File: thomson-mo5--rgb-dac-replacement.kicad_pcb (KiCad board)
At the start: 2 copper layers, 0 parts

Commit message: Done PCB
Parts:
- added J1: Input, Connector_PinHeader_2.54mm:PinHeader_1x09_P2.54mm_Vertical, F.Cu at (158.8, 76.2)
- added J2: Output, Connector_PinHeader_2.54mm:PinHeader_1x03_P2.54mm_Vertical, F.Cu at (74.9, 78.7)
- added Q1: 2N3904, Package_TO_SOT_THT:TO-92_Inline_Wide, F.Cu at (125.7, 99.1)
- added Q2: 2N3904, Package_TO_SOT_THT:TO-92_Inline_Wide, F.Cu at (110.5, 99.1)
- added Q3: 2N3904, Package_TO_SOT_THT:TO-92_Inline_Wide, F.Cu at (95.2, 99.1)
- added R1: 1K5, commons-passives_THT:Passive_THT_resistor_W2.54mm_L12.70mm, F.Cu at (130.8, 85.1)
- added R10: 3K, commons-passives_THT:Passive_THT_resistor_W2.54mm_L12.70mm, F.Cu at (102.9, 85.1)
- added R11: 6K2, commons-passives_THT:Passive_THT_resistor_W2.54mm_L12.70mm, F.Cu at (100.3, 85.1)
- added R12: 12K, commons-passives_THT:Passive_THT_resistor_W2.54mm_L12.70mm, F.Cu at (97.8, 85.1)
- added R13: 1K, commons-passives_THT:Passive_THT_resistor_W2.54mm_L12.70mm, F.Cu at (132.1, 103.5)
- added R14: 1K, commons-passives_THT:Passive_THT_resistor_W2.54mm_L12.70mm, F.Cu at (116.8, 103.5)
- added R15: 1K, commons-passives_THT:Passive_THT_resistor_W2.54mm_L12.70mm, F.Cu at (101.6, 103.5)
- added R16: 2K, commons-passives_THT:Passive_THT_resistor_W2.54mm_L12.70mm, F.Cu at (132.1, 106.0)
- added R17: 2K, commons-passives_THT:Passive_THT_resistor_W2.54mm_L12.70mm, F.Cu at (116.8, 106.0)
- added R18: 2K, commons-passives_THT:Passive_THT_resistor_W2.54mm_L12.70mm, F.Cu at (101.6, 106.0)
- added R19: 150, commons-passives_THT:Passive_THT_resistor_W2.54mm_L12.70mm, F.Cu at (132.1, 108.6)
- added R2: 3K, commons-passives_THT:Passive_THT_resistor_W2.54mm_L12.70mm, F.Cu at (128.3, 85.1)
- added R20: 150, commons-passives_THT:Passive_THT_resistor_W2.54mm_L12.70mm, F.Cu at (116.8, 108.6)
- added R21: 150, commons-passives_THT:Passive_THT_resistor_W2.54mm_L12.70mm, F.Cu at (101.6, 108.6)
- added R22: 75, commons-passives_THT:Passive_THT_resistor_W2.54mm_L12.70mm, F.Cu at (92.7, 85.1)
- added R23: 75, commons-passives_THT:Passive_THT_resistor_W2.54mm_L12.70mm, F.Cu at (90.2, 85.1)
- added R24: 75, commons-passives_THT:Passive_THT_resistor_W2.54mm_L12.70mm, F.Cu at (87.6, 85.1)
- added R3: 6K2, commons-passives_THT:Passive_THT_resistor_W2.54mm_L12.70mm, F.Cu at (125.7, 85.1)
- added R4: 12K, commons-passives_THT:Passive_THT_resistor_W2.54mm_L12.70mm, F.Cu at (123.2, 85.1)
- added R5: 1K5, commons-passives_THT:Passive_THT_resistor_W2.54mm_L12.70mm, F.Cu at (118.1, 85.1)
- added R6: 3K, commons-passives_THT:Passive_THT_resistor_W2.54mm_L12.70mm, F.Cu at (115.6, 85.1)
- added R7: 6K2, commons-passives_THT:Passive_THT_resistor_W2.54mm_L12.70mm, F.Cu at (113.0, 85.1)
- added R8: 12K, commons-passives_THT:Passive_THT_resistor_W2.54mm_L12.70mm, F.Cu at (110.5, 85.1)
- added R9: 1K5, commons-passives_THT:Passive_THT_resistor_W2.54mm_L12.70mm, F.Cu at (105.4, 85.1)
- added U1: QUADRUPLE_2-INPUTS_POSITIVE-OR_GATES, Package_DIP:DIP-14_W7.62mm_LongPads, F.Cu at (141.0, 80.0)
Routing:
- net GND: track 0.00 -> 128.9 mm, vias 0 -> 15
- net +5V: track 0.00 -> 117.1 mm, vias 0 -> 6
- net /B2: track 0.00 -> 69.6 mm, vias 0 -> 5
- net /B1: track 0.00 -> 68.9 mm, vias 0 -> 3
- net /B0: track 0.00 -> 65.8 mm, vias 0 -> 3
- net Net-(Q1-E): track 0.00 -> 61.4 mm, vias 0 -> 3
- net /G1: track 0.00 -> 51.5 mm, vias 0 -> 3
- net /G2: track 0.00 -> 51.5 mm, vias 0 -> 3
- net Net-(Q2-E): track 0.00 -> 47.2 mm, vias 0 -> 2
- net /G0: track 0.00 -> 43.3 mm, vias 0 -> 3
- net Net-(Q3-E): track 0.00 -> 36.0 mm, vias 0 -> 2
- net Net-(Q2-B): track 0.00 -> 34.9 mm, vias 0 -> 2
- net Net-(Q1-B): track 0.00 -> 34.9 mm, vias 0 -> 2
- net Net-(Q3-B): track 0.00 -> 34.9 mm, vias 0 -> 2
- net /R1: track 0.00 -> 32.6 mm
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- added copper zone on B.Cu, net GND
- added copper zone on F.Cu, net GND
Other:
- board outline added: 91.4 x 41.9 mm
- board text added: "B1"
- board text added: "B2"
- board text added: "BLUE"
- board text added: "G1"
- board text added: "G2"
- board text added: "GND"
- board text added: "GREEN"
- board text added: "NC"
- board text added: "R1"
- board text added: "R2"
- board text added: "RED"
- board text added: "VCC"

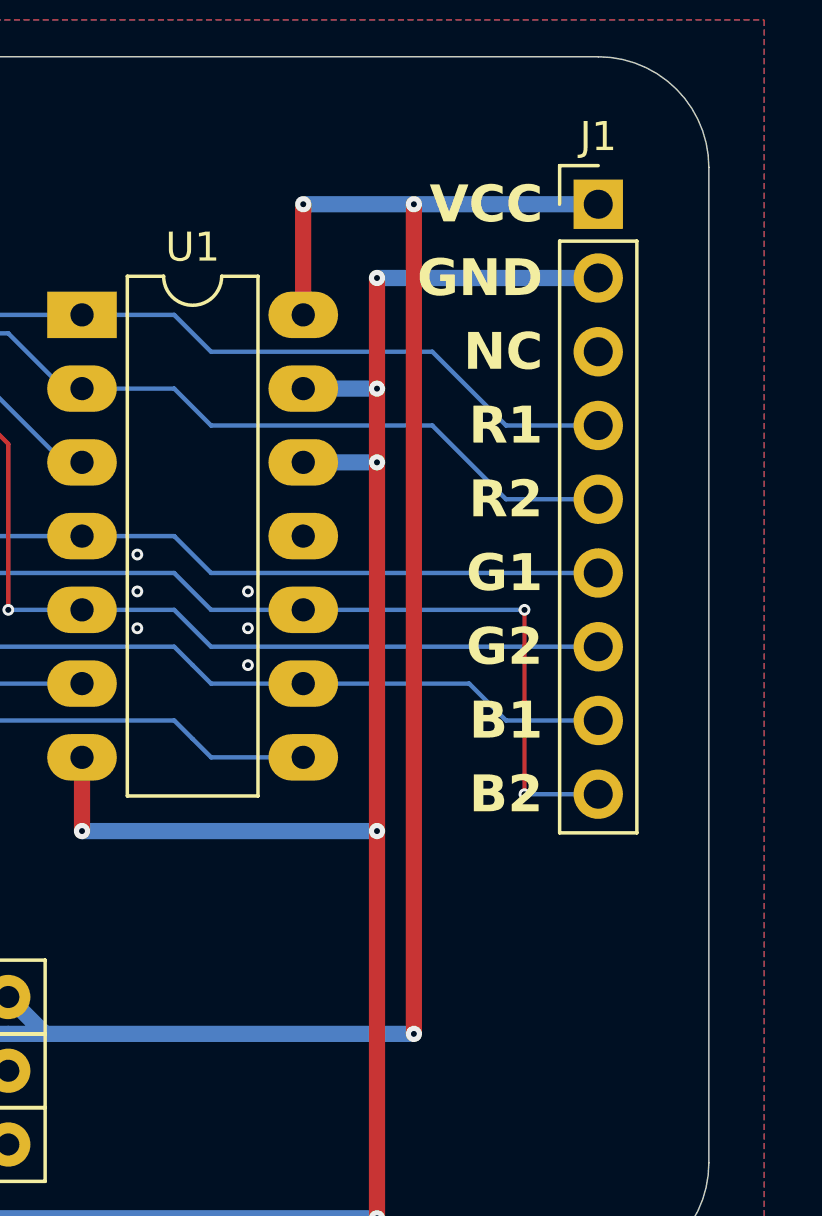
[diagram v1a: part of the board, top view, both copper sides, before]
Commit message: Added decoupling capacitor
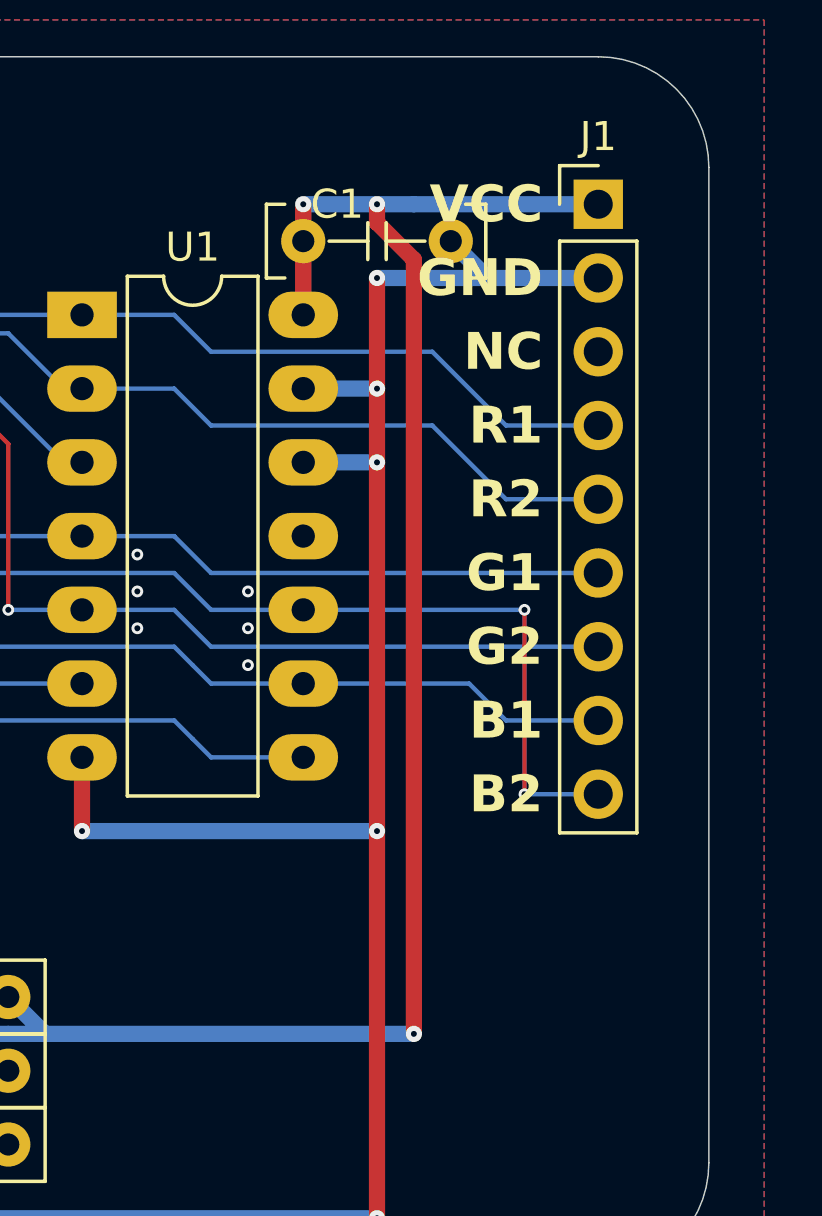
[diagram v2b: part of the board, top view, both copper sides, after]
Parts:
- added C1: 0.1uF, commons-passives_THT:Passive_THT_capacitor_mlcc_W2.54mm_L5.08mm, F.Cu at (151.1, 77.5)
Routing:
- net GND: track 128.9 -> 130.7 mm
- net +5V: track 117.1 -> 117.7 mm
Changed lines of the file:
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@@
     )
+  )
+  (footprint "commons-passives_THT:Passive_THT_capacitor_mlcc_W2.54mm_L5.08mm" (layer "F.Cu")
+    (at 151.13 77.47)
+    (descr "MLCC THT radial capacitor, width 100mils, lead vias 200mils apart")
+    (tags "mlcc radial capacitor tht")
+    (property "Sheetfile" "thomson-mo5--rgb-dac-replacement.kicad_sch")
+    (property "Sheetname" "")
+    (property "ki_description" "Unpolarized capacitor, small symbol")
+    (property "ki_keywords" "capacitor cap")
+    (attr through_hole)
+    (fp_text reference "C1" (at -2.286 -1.27) (layer "F.SilkS")
+        (effects (font (size 1 1) (thickness 0.15)) (justify left))
+    )
+    (fp_text value "0.1uF" (at 0 -0.5) (layer "F.Fab")
+        (effects (font (size 1 1) (thickness 0.15)))
+    )
+    (fp_line (start -3.81 -1.27) (end -3.175 -1.27)
+      (stroke (width 0.12) (type solid)) (layer "F.SilkS"))
+    (fp_line (start -3.81 1.27) (end -3.81 -1.27)
+      (stroke (width 0.12) (type solid)) (layer "F.SilkS"))
+    (fp_line (start -3.175 1.27) (end -3.81 1.27)
+      (stroke (width 0.12) (type solid)) (layer "F.SilkS"))
+    (fp_line (start -1.651 0) (end -0.3175 0)
+      (stroke (width 0.12) (type solid)) (layer "F.SilkS"))
+    (fp_line (start -0.3175 -0.635) (end -0.3175 0.635)
+      (stroke (width 0.12) (type solid)) (layer "F.SilkS"))
+    (fp_line (start 0.3175 -0.635) (end 0.3175 0.635)
+      (stroke (width 0.12) (type solid)) (layer "F.SilkS"))
+    (fp_line (start 0.3175 0) (end 1.651 0)
+      (stroke (width 0.12) (type solid)) (layer "F.SilkS"))
+    (fp_line (start 3.048 -1.27) (end 3.7465 -1.27)
+      (stroke (width 0.12) (type solid)) (layer "F.SilkS"))
+    (fp_line (start 3.7465 -1.27) (end 3.7465 1.27)
+      (stroke (width 0.12) (type solid)) (layer "F.SilkS"))
+    (fp_line (start 3.7465 1.27) (end 3.048 1.27)
+      (stroke (width 0.12) (type solid)) (layer "F.SilkS"))
+    (pad "1" thru_hole circle (at -2.54 0) (size 1.524 1.524) (drill 0.762) (layers "*.Cu" "*.Mask")
+      (net 1 "+5V") (pintype "passive"))
+    (pad "2" thru_hole circle (at 2.54 0) (size 1.524 1.524) (drill 0.762) (layers "*.Cu" "*.Mask")
+      (net 2 "GND") (pintype "passive"))
   )
   (footprint "commons-passives_THT:Passive_THT_resistor_W2.54mm_L12.70mm" (layer "F.Cu")
@@
   )
   (segment (start 115.57 99.06) (end 115.57 104.775) (width 0.5588) (layer "F.Cu") (net 1))
-  (segment (start 152.4 104.775) (end 152.4 76.2) (width 0.5588) (layer "F.Cu") (net 1))
+  (segment (start 148.59 76.2) (end 148.59 77.47) (width 0.5588) (layer "F.Cu") (net 1))
+  (segment (start 152.4 104.775) (end 152.4 78.105) (width 0.5588) (layer "F.Cu") (net 1))
+  (segment (start 151.13 76.835) (end 151.13 76.2) (width 0.5588) (layer "F.Cu") (net 1))
+  (segment (start 148.59 80.01) (end 148.59 77.47) (width 0.5588) (layer "F.Cu") (net 1))
   (segment (start 100.33 99.06) (end 100.33 104.775) (width 0.5588) (layer "F.Cu") (net 1))
-  (segment (start 148.59 76.2) (end 148.59 80.01) (width 0.5588) (layer "F.Cu") (net 1))
+  (segment (start 152.4 78.105) (end 151.13 76.835) (width 0.5588) (layer "F.Cu") (net 1))
   (segment (start 130.81 99.06) (end 130.81 104.775) (width 0.5588) (layer "F.Cu") (net 1))
+  (via (at 151.13 76.2) (size 0.5588) (drill 0.2032) (layers "F.Cu" "B.Cu") (net 1))
   (via (at 100.33 104.775) (size 0.5588) (drill 0.2032) (layers "F.Cu" "B.Cu") (net 1))
   (via (at 115.57 104.775) (size 0.5588) (drill 0.2032) (layers "F.Cu" "B.Cu") (net 1))
   (via (at 148.59 76.2) (size 0.5588) (drill 0.2032) (layers "F.Cu" "B.Cu") (net 1))
   (via (at 152.4 104.775) (size 0.5588) (drill 0.2032) (layers "F.Cu" "B.Cu") (net 1))
-  (via (at 152.4 76.2) (size 0.5588) (drill 0.2032) (layers "F.Cu" "B.Cu") (net 1))
   (via (at 130.81 104.775) (size 0.5588) (drill 0.2032) (layers "F.Cu" "B.Cu") (net 1))
   (segment (start 123.19 103.505) (end 124.46 104.775) (width 0.5588) (layer "B.Cu") (net 1))
@@
   (segment (start 138.43 103.505) (end 139.7 104.775) (width 0.5588) (layer "B.Cu") (net 1))
   (segment (start 109.22 104.775) (end 107.95 103.505) (width 0.5588) (layer "B.Cu") (net 1))
-  (segment (start 152.4 76.2) (end 148.59 76.2) (width 0.5588) (layer "B.Cu") (net 1))
   (segment (start 124.46 104.775) (end 123.19 104.775) (width 0.5588) (layer "B.Cu") (net 1))
   (segment (start 158.75 76.2) (end 152.4 76.2) (width 0.5588) (layer "B.Cu") (net 1))
   (segment (start 125.095 104.775) (end 130.81 104.775) (width 0.5588) (layer "B.Cu") (net 1))
+  (segment (start 152.4 76.2) (end 151.13 76.2) (width 0.5588) (layer "B.Cu") (net 1))
   (segment (start 139.7 104.775) (end 152.4 104.775) (width 0.5588) (layer "B.Cu") (net 1))
   (segment (start 124.46 104.775) (end 125.095 104.775) (width 0.5588) (layer "B.Cu") (net 1))
@@
   (segment (start 123.19 104.775) (end 115.57 104.775) (width 0.5588) (layer "B.Cu") (net 1))
   (segment (start 100.33 104.775) (end 109.22 104.775) (width 0.5588) (layer "B.Cu") (net 1))
+  (segment (start 151.13 76.2) (end 148.59 76.2) (width 0.5588) (layer "B.Cu") (net 1))
   (segment (start 138.43 104.775) (end 139.7 104.775) (width 0.5588) (layer "B.Cu") (net 1))
   (segment (start 110.49 108.585) (end 110.49 111.125) (width 0.5588) (layer "F.Cu") (net 2))
@@
   (via (at 151.13 85.09) (size 0.5588) (drill 0.2032) (layers "F.Cu" "B.Cu") (net 2))
   (segment (start 151.13 111.125) (end 125.73 111.125) (width 0.5588) (layer "B.Cu") (net 2))
-  (segment (start 158.75 78.74) (end 151.13 78.74) (width 0.5588) (layer "B.Cu") (net 2))
   (segment (start 125.73 111.125) (end 110.49 111.125) (width 0.5588) (layer "B.Cu") (net 2))
   (segment (start 110.49 111.125) (end 95.25 111.125) (width 0.5588) (layer "B.Cu") (net 2))
+  (segment (start 153.67 77.47) (end 154.94 78.74) (width 0.5588) (layer "B.Cu") (net 2))
+  (segment (start 154.94 78.74) (end 151.13 78.74) (width 0.5588) (layer "B.Cu") (net 2))
+  (segment (start 158.75 78.74) (end 154.94 78.74) (width 0.5588) (layer "B.Cu") (net 2))
   (segment (start 151.13 85.09) (end 148.59 85.09) (width 0.5588) (layer "B.Cu") (net 2))
   (segment (start 148.59 82.55) (end 151.13 82.55) (width 0.5588) (layer "B.Cu") (net 2))

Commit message: finalized pcb
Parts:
- added G***: LOGO, cliparts:logo--cc--zero, F.Cu at (158.8, 109.2)
- added G***: LOGO, cliparts:logo--cc--cc, F.Cu at (154.3, 109.2)
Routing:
- net /R0: track 20.4 -> 24.9 mm, vias 0 -> 2
- net /R2: track 32.2 -> 36.0 mm
- net /VID_RED: track 22.1 -> 20.3 mm
- net /VID_GREEN: track 18.8 -> 17.0 mm
- net /G2: track 51.5 -> 53.2 mm
- net /G1: track 51.5 -> 52.6 mm
- net /G0: track 43.3 -> 44.5 mm
- net /B0: track 65.8 -> 66.6 mm
- net /B2: track 69.6 -> 70.4 mm
- net /B1: track 68.9 -> 69.6 mm
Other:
- board text added: "${COMMENT3}"
- board text added: "${REVISION} - ${ISSUE_DATE}"
- board text added: "${TITLE}"
- board text added: "WITHOUT ANY WARRANTY; without even the implied warranty of SAFETY, MERCHANTABILITY or FITNESS FOR A PARTICULAR PURPOSE."

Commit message: Final tunings in layout (schematic and pcb)
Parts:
- moved C1 5.24 mm to (146.1, 76.2), turned to 180 degrees
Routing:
- net GND: track 130.7 -> 140.6 mm, vias 15 -> 16
- net /R2: track 36.0 -> 32.8 mm
- net /VID_GREEN: track 17.0 -> 16.3 mm, vias 1 -> 0
- net +5V: track 117.7 -> 117.1 mm, vias 6 -> 5

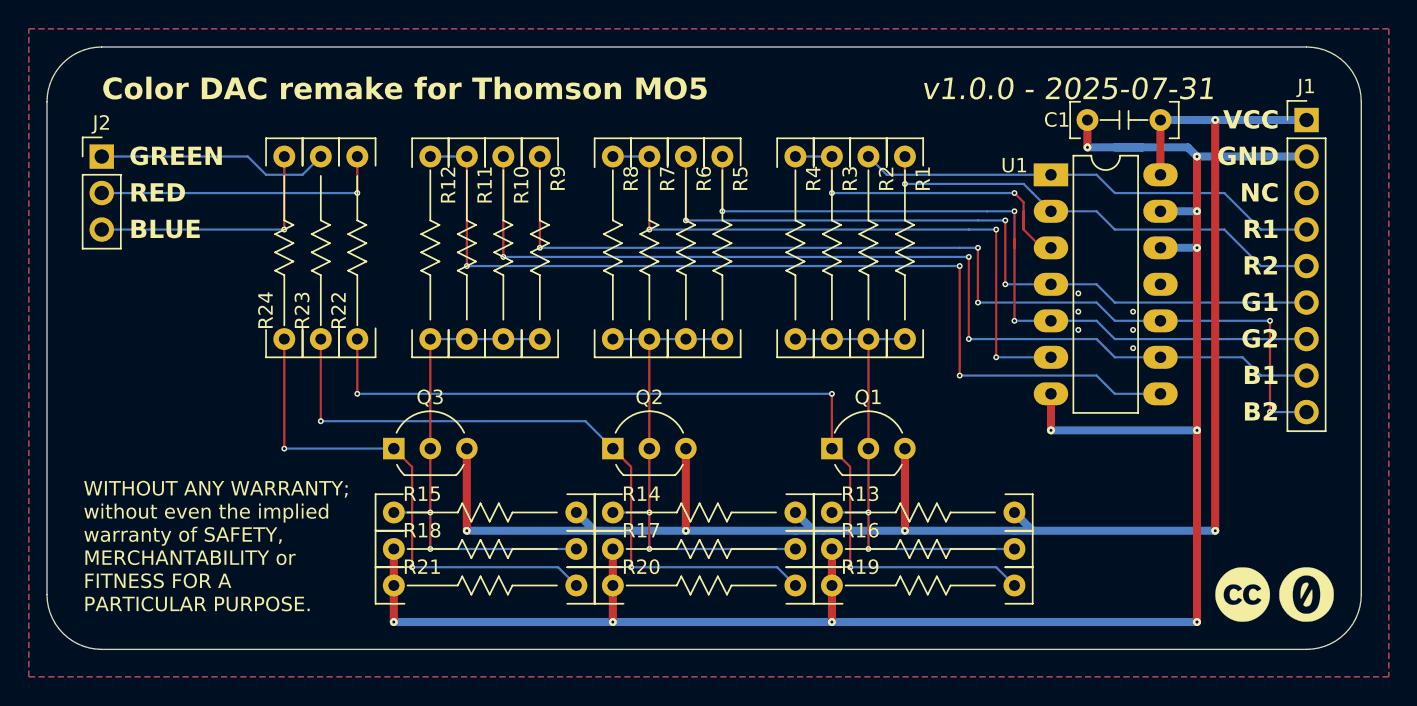
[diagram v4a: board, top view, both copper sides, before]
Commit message: [pcb] applied schematic change, and shrinked the required size
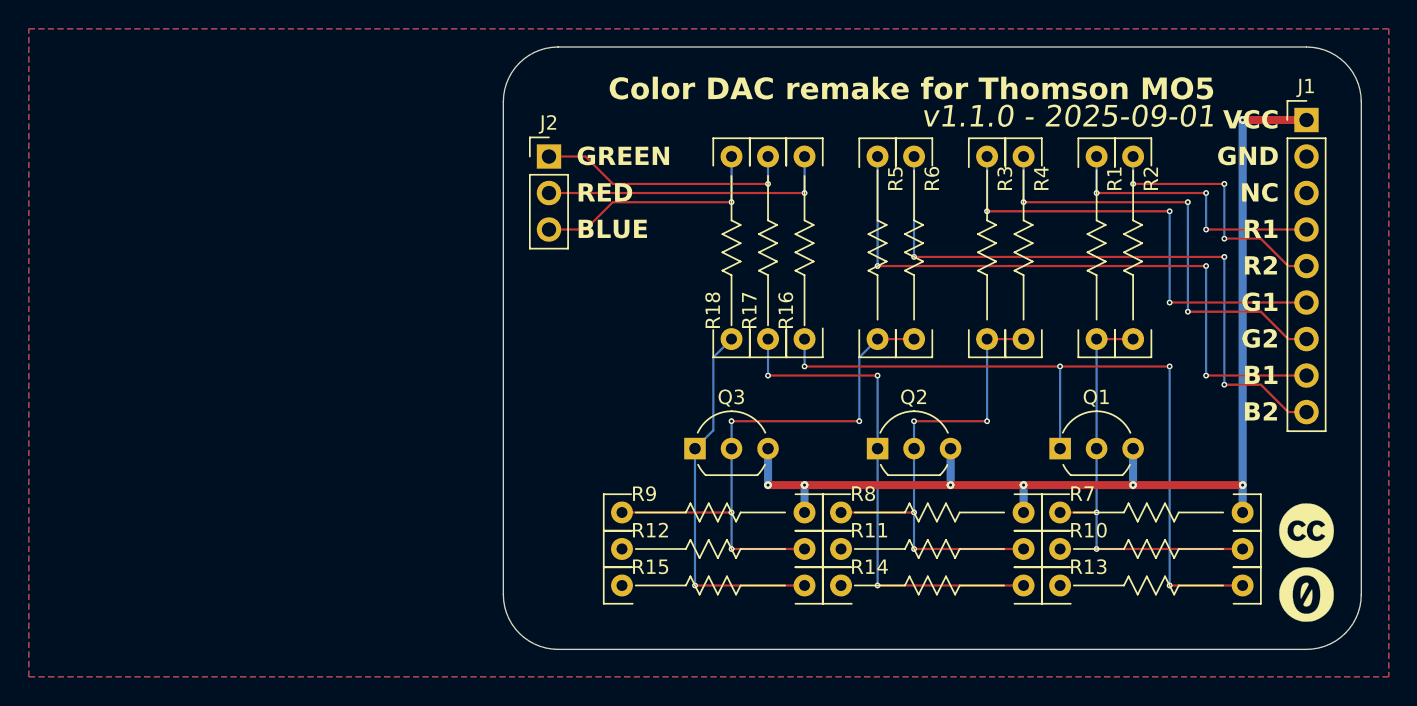
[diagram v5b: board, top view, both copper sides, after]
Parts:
- removed C1: 0.1uF, commons-passives_THT:Passive_THT_capacitor_mlcc_W2.54mm_L5.08mm
- removed the R11 at (100.3, 85.1)
- removed the R12 at (97.8, 85.1)
- removed the R3 at (125.7, 85.1)
- removed the R4 at (123.2, 85.1)
- removed the R7 at (113.0, 85.1)
- removed the R8 at (110.5, 85.1)
- removed U1: QUADRUPLE_2-INPUTS_POSITIVE-OR_GATES, Package_DIP:DIP-14_W7.62mm_LongPads
- R1: renamed from R2; value 3K -> 2K4
- R2: renamed from R1; value 1K5 -> 1K2
- R3: renamed from R6; value 3K -> 2K4
- R4: renamed from R5; value 1K5 -> 1K2
- R5: renamed from R10; value 3K -> 2K4
- R6: renamed from R9; value 1K5 -> 1K2
- moved R16 31.1 mm to (123.8, 85.1)
- moved R18 31.1 mm to (118.7, 85.1)
- moved J2 31.1 mm to (106.0, 78.7)
- moved R17 31.1 mm to (121.3, 85.1)
- moved R5 26.0 mm to (128.9, 85.1)
- moved R6 26.0 mm to (131.4, 85.1)
- moved R3 21.0 mm to (136.5, 85.1)
- moved Q3 21.0 mm to (116.2, 99.1)
- moved R4 21.0 mm to (139.1, 85.1)
- moved Q2 18.4 mm to (128.9, 99.1)
- moved R1 15.9 mm to (144.1, 85.1)
- moved R10 15.9 mm to (148.0, 106.0)
- moved R11 15.9 mm to (132.7, 106.0)
- moved R12 15.9 mm to (117.5, 106.0)
- moved R13 15.9 mm to (148.0, 108.6)
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- renumbered R16 to R10, R17 to R11, R18 to R12, R19 to R13, R20 to R14, R21 to R15, R22 to R16, R23 to R17, R24 to R18, R13 to R7, R14 to R8, R15 to R9
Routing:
- net GND: track 140.6 -> 0.00 mm, vias 16 -> 0
- net /B0: track 66.6 -> 0.00 mm, vias 3 -> 0
- net /G0: track 44.5 -> 0.00 mm, vias 3 -> 0
- net +5V: track 117.1 -> 76.2 mm, vias 5 -> 7
- net /B2: track 70.4 -> 44.0 mm, vias 5 -> 3
- net /R0: track 24.9 -> 0.00 mm, vias 2 -> 0
- net /B1: track 69.6 -> 45.1 mm
- net /G2: track 53.2 -> 31.3 mm
- net /G1: track 52.6 -> 32.4 mm
- net /R2: track 32.8 -> 18.6 mm, vias 1 -> 3
- net /R1: track 32.6 -> 19.7 mm, vias 0 -> 3
- net Net-(Q2-E): track 47.6 -> 34.9 mm, vias 2 -> 3
- net Net-(Q3-E): track 36.0 -> 25.8 mm, vias 2 -> 1
- net Net-(Q1-E): track 61.4 -> 53.3 mm, vias 3 -> 4
- net Net-(Q1-B): track 34.9 -> 29.8 mm
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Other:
- board size 91.4 x 41.9 mm -> 59.7 x 41.9 mm
